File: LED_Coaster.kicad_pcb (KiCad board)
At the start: 2 copper layers, 90 x 90 mm, 60 parts, among them J1 USB_C_Receptacle_USB2.0, SW1 SW_Push, SW2 SW_DIP_x01, SW3 SW_DIP_x01, U1 ATmega32U4-A, Y1 Crystal_GND24

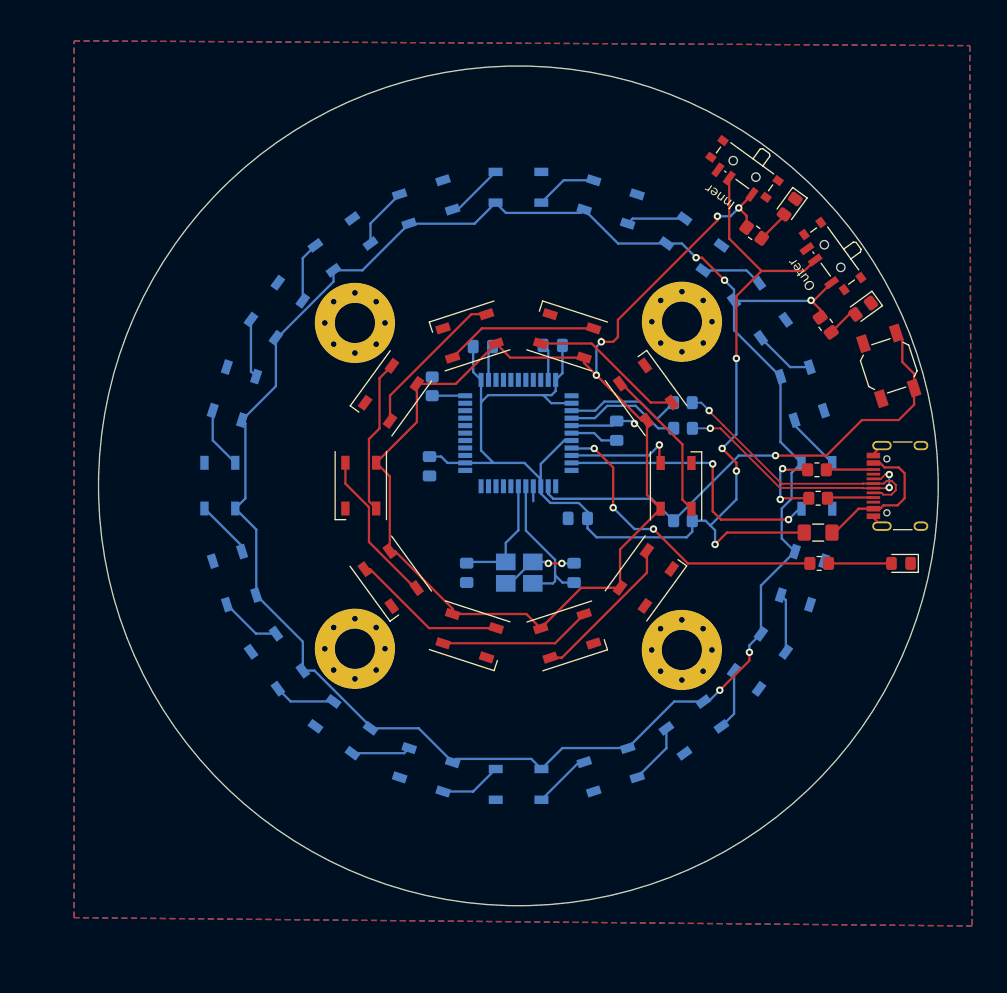
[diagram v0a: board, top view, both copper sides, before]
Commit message: Version 3 using esp32-C3
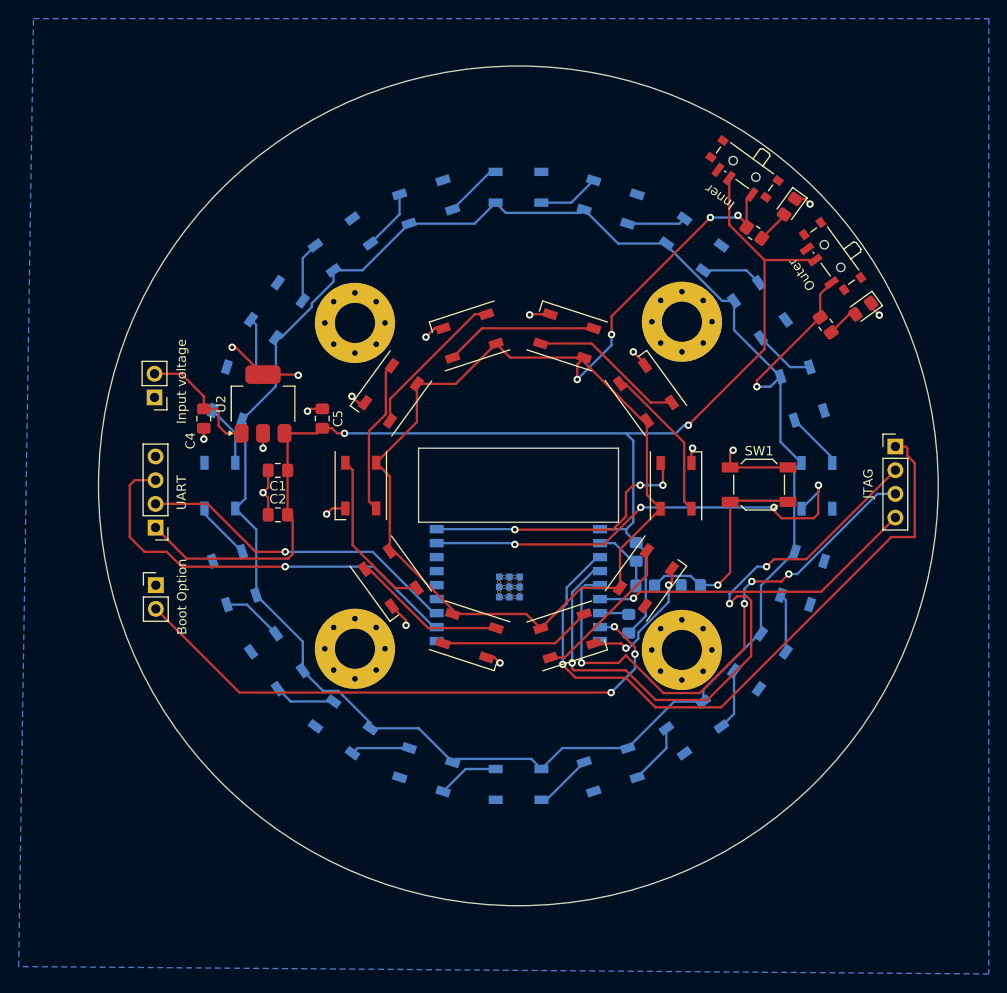
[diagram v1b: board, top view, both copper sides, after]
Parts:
- removed C6, C7: 22pF, Capacitor_SMD:C_0805_2012Metric_Pad1.18x1.45mm_HandSolder
- removed D33: LED, LED_SMD:LED_0805_2012Metric_Pad1.15x1.40mm_HandSolder
- removed F1: Polyfuse, Fuse:Fuse_1206_3216Metric_Pad1.42x1.75mm_HandSolder
- removed R2: 22, Resistor_SMD:R_0805_2012Metric_Pad1.20x1.40mm_HandSolder
- removed R5, R6: 5.1K, Resistor_SMD:R_0805_2012Metric_Pad1.20x1.40mm_HandSolder
- removed R9: 150, Resistor_SMD:R_0805_2012Metric_Pad1.20x1.40mm_HandSolder
- removed Y1: Crystal_GND24, Crystal:Crystal_SMD_3225-4Pin_3.2x2.5mm_HandSoldering
- added J2: Boot Option, Connector_PinHeader_2.54mm:PinHeader_1x02_P2.54mm_Vertical, F.Cu at (111.1, 90.6)
- added J3: JTAG, Connector_PinHeader_2.54mm:PinHeader_1x04_P2.54mm_Vertical, F.Cu at (190.4, 75.8)
- added J4: UART, Connector_PinHeader_2.54mm:PinHeader_1x04_P2.54mm_Vertical, F.Cu at (111.1, 84.5)
- added U2: MCP1792x-3302xDB, Package_TO_SOT_SMD:SOT-223-3_TabPin2, F.Cu at (122.6, 71.2)
- C1: value 1uF -> 10uF; moved to F.Cu
- C2: value 10uF -> 0.1uF; moved to F.Cu
- C3: value 0.1uF -> 1uF
- C4, C5: value 0.1uF -> 2.2uF; moved to F.Cu
- J1: value USB_C_Receptacle_USB2.0 -> Input voltage; footprint Connector_USB:USB_C_Receptacle_HRO_TYPE-C-31-M-12 -> Connector_PinHeader_2.54mm:PinHeader_1x02_P2.54mm_Vertical
- R1, R4: value 10K -> 10k
- R3: value 22 -> 10k
- SW1: value SW_Push -> SW_SPST; footprint Button_Switch_SMD:SW_SPST_SKQG_WithoutStem -> Button_Switch_SMD:SW_SPST_SKQG_WithStem
- U1: value ATmega32U4-A -> ESP32-C3-WROOM-02-H4; footprint Package_QFP:TQFP-44_10x10mm_P0.8mm -> ESP32-C3-WROOM-02-H4:MODULE_ESP32-C3-WROOM-02-H4
- moved J1 81.6 mm to (111.0, 70.5), turned to 180 degrees
- moved C4 41.5 mm to (116.3, 72.8), turned to 90 degrees
- moved C1 36.6 mm to (124.2, 78.3), turned to 180 degrees
- moved C2 34.6 mm to (124.2, 83.1), turned to 0 degrees
- moved C3 34.0 mm to (168.5, 90.7)
- moved R1 31.3 mm to (163.6, 90.7), turned to 180 degrees
- moved SW1 18.8 mm to (175.8, 79.9), turned to 0 degrees
- moved R3 16.8 mm to (162.6, 87.1), turned to -90 degrees
- moved U1 13.2 mm to (150.0, 87.5)
- moved C5 12.6 mm to (129.0, 72.8)
- moved R4 12.5 mm to (161.8, 94.8), turned to 90 degrees
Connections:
- C1 pad 1: Net-(U1-UCAP) -> +3V3
- C2 pad 1: +5V -> GND
- C2 pad 2: GND -> +3V3
- C3 pad 1: +5V -> GND
- C3 pad 2: GND -> Net-(SW1-B)
- C4 pad 1: +5V -> GND
- C4 pad 2: GND -> +5V
- C5 pad 1: +5V -> GND
- C5 pad 2: GND -> +3V3
- R1 pad 1: Net-(U1-~{HWB}/PE2) -> Net-(SW1-B)
- R1 pad 2: GND -> Net-(U1-EN)
- R3 pad 1: /D- -> +3V3
- R3 pad 2: Net-(U1-D-) -> Net-(U1-EN)
- R4 pad 1: Net-(U1-~{RESET}) -> +3V3
- R4 pad 2: +5V -> Net-(U1-IO8)
- SW1 pad 2: Net-(U1-~{RESET}) -> Net-(SW1-B)
- SW2 pad 2: +5V -> +3V3
- SW3 pad 2: +5V -> +3V3
- U1 pad 1: unconnected-(U1-PE6-Pad1) -> +3V3
- U1 pad 10: /large_ring -> unconnected-(U1-IO10-Pad10)
- U1 pad 11: unconnected-(U1-PB3-Pad11) -> Net-(J4-Pin_3)
- U1 pad 12: unconnected-(U1-PB7-Pad12) -> Net-(J4-Pin_2)
- U1 pad 13: Net-(U1-~{RESET}) -> unconnected-(U1-IO18-Pad13)
- U1 pad 14: +5V -> unconnected-(U1-IO19-Pad14)
- U1 pad 15: GND -> unconnected-(U1-IO3-Pad15)
- U1 pad 16: Net-(U1-XTAL2) -> unconnected-(U1-IO2-Pad16)
- U1 pad 17: Net-(U1-XTAL1) -> /large_ring
- U1 pad 18: unconnected-(U1-PD0-Pad18) -> /small_ring
- U1 pad 19: unconnected-(U1-PD1-Pad19) -> GND
- U1 pad 2: +5V -> Net-(U1-EN)
- U1 pad 20: unconnected-(U1-PD2-Pad20) -> GND
- U1 pad 21: unconnected-(U1-PD3-Pad21) -> GND
- U1 pad 22: unconnected-(U1-PD5-Pad22) -> GND
- U1 pad 24: +5V -> GND
- U1 pad 25: unconnected-(U1-PD4-Pad25) -> GND
- U1 pad 26: unconnected-(U1-PD6-Pad26) -> GND
- U1 pad 27: unconnected-(U1-PD7-Pad27) -> GND
- U1 pad 28: unconnected-(U1-PB4-Pad28) -> GND
- U1 pad 29: unconnected-(U1-PB5-Pad29) -> GND
- U1 pad 3: Net-(U1-D-) -> Net-(J3-Pin_1)
- U1 pad 30: unconnected-(U1-PB6-Pad30) -> GND
- U1 pad 31: unconnected-(U1-PC6-Pad31) -> GND
- U1 pad 32: unconnected-(U1-PC7-Pad32) -> GND
- U1 pad 33: Net-(U1-~{HWB}/PE2) -> GND
- U1 pad 34: +5V -> GND
- U1 pad 36: unconnected-(U1-PF7-Pad36) -> GND
- U1 pad 37: unconnected-(U1-PF6-Pad37) -> GND
- U1 pad 38: unconnected-(U1-PF5-Pad38) -> GND
- U1 pad 39: unconnected-(U1-PF4-Pad39) -> GND
- U1 pad 5: GND -> Net-(J3-Pin_3)
- U1 pad 6: Net-(U1-UCAP) -> Net-(J3-Pin_4)
- U1 pad 7: +5V -> Net-(U1-IO8)
- U1 pad 9: /small_ring -> GND
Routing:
- net +3V3: track 0.00 -> 137.0 mm, vias 0 -> 2
- net +5V: track 135.2 -> 13.7 mm, vias 4 -> 0
- net Net-(J3-Pin_1): track 0.00 -> 71.8 mm, vias 0 -> 1
- net Net-(J3-Pin_3): track 0.00 -> 58.3 mm, vias 0 -> 4
- net Net-(J3-Pin_2): track 12.5 -> 67.7 mm, vias 0 -> 3
- net Net-(U1-~{RESET}): track 55.0 -> 0.00 mm, vias 1 -> 0
- net Net-(J4-Pin_3): track 0.00 -> 45.4 mm, vias 0 -> 1
- net Net-(J3-Pin_4): track 0.00 -> 35.3 mm, vias 0 -> 1
- net Net-(J4-Pin_2): track 0.00 -> 35.0 mm, vias 0 -> 1
- net Net-(J2-Pin_2): track 33.2 -> 63.1 mm
- net /D-: track 29.0 -> 0.00 mm, vias 1 -> 0
- net /D+: track 27.1 -> 0.00 mm, vias 3 -> 0
- net Net-(SW1-B): track 0.00 -> 23.5 mm, vias 0 -> 1
- net GND: track 37.8 -> 61.0 mm, vias 5 -> 19
- net /large_ring: track 30.8 -> 49.8 mm, vias 2 -> 4
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- removed copper zone on F.Cu, net GND
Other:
- outline, holes or cut-outs redrawn
